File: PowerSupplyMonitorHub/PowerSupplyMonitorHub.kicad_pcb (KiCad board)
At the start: 2 copper layers, 145 x 62 mm, 97 parts, among them J1 PCA, J10 Input, J2 RJ45 PWR 0, J3 RJ45 PWR 1, J4 RJ45 PWR 2, J5 RJ45 PWR 3, J6 RJ45 PWR 4, J7 OLED I2C, J8 TCA, J9 PCF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

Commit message: added minimal readme
added many vias for ground front and back plane
updated 3d render of i2c hub pcb
updated gerber archive files
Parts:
- moved C1 1.14 mm to (108.6, 118.9), turned to 270 degrees
- moved C3 0.64 mm to (200.9, 118.2)
- turned R13 to 180 degrees
- turned R14 to 180 degrees
- turned R15 to 180 degrees
- turned R9 to 180 degrees
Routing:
- net +5V: track 467.5 -> 447.7 mm, vias 2 -> 3
- net /LINK_4: track 156.8 -> 170.0 mm, vias 0 -> 2
- net /DC-OK_0: track 33.3 -> 25.2 mm, vias 0 -> 2
- net GND: track 0.00 -> 7.65 mm, vias 0 -> 29
- net Net-(J8-Pad3): track 14.7 -> 7.96 mm, vias 0 -> 1
- net /RC_3: track 49.3 -> 56.0 mm
- net /DC-OK_4: track 19.9 -> 24.8 mm
- net /RC_1: track 22.8 -> 27.5 mm
- net Net-(J8-Pad5): track 13.2 -> 8.60 mm, vias 0 -> 1
- net /DATA_3: track 109.3 -> 113.7 mm
- net /DC-OK_1: track 20.0 -> 24.3 mm, vias 0 -> 2
- net /DATA_4: track 175.7 -> 179.6 mm
- net /RC_0: track 47.1 -> 43.2 mm, vias 0 -> 2
- net /SDA1: track 68.5 -> 72.0 mm
- net /SCL0: track 94.5 -> 97.8 mm
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
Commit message: updated readme and license file
added datasheet for ads1015
added datasheet for pca9685
added foto of gy-712 30a sensor
added small changes to pcbs
updated 3d render of pcbs
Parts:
- turned R15 to 0 degrees
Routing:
- net +5V: track 447.7 -> 428.9 mm, vias 3 -> 4
- net /LINK_4: track 170.0 -> 175.1 mm
- net /RC_4: track 78.1 -> 73.6 mm, vias 0 -> 2
- net /DC-OK_4: track 24.8 -> 22.9 mm
- net /RC_2: track 25.5 -> 27.3 mm
- net Net-(R15-Pad2): track 4.13 -> 3.28 mm
- net /SDA: track 177.2 -> 177.9 mm

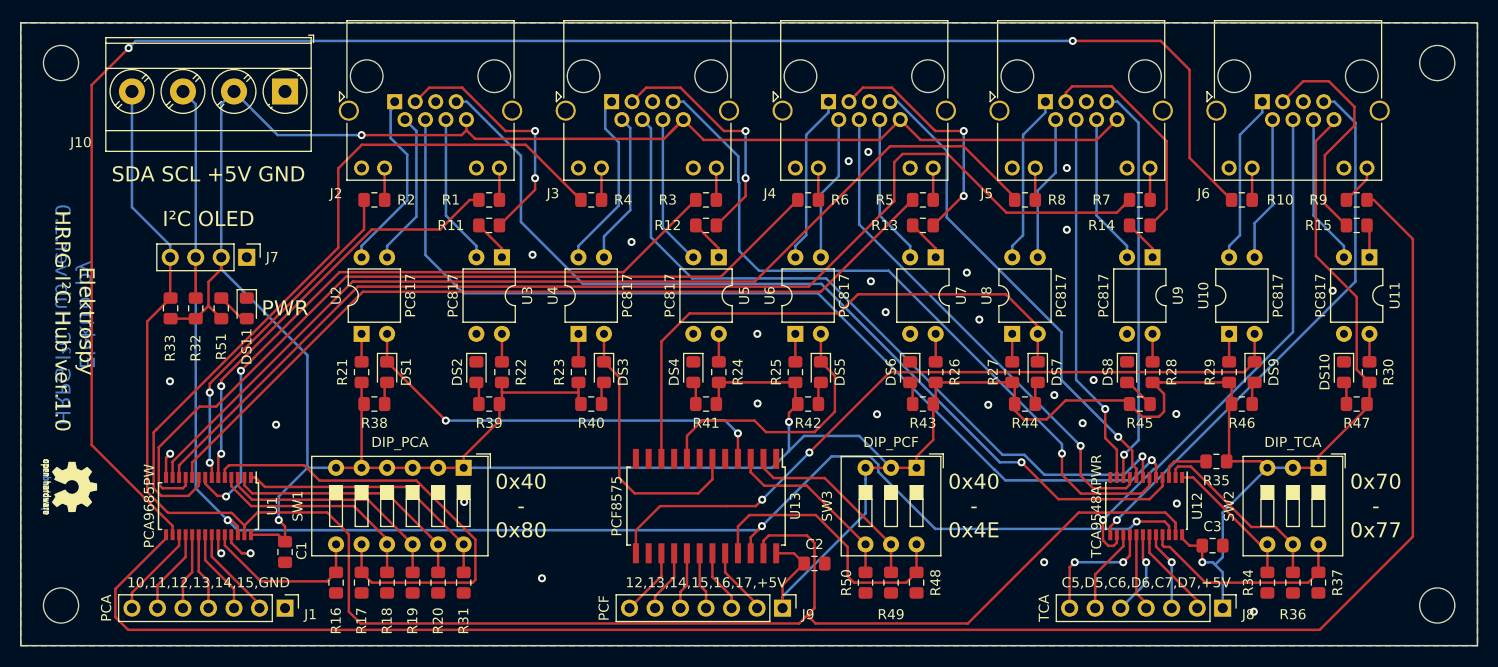
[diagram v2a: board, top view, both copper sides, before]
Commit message: fixed pcb errors
swapped gnd and vcc pin of 4 position switch to fix first two addresses
added custom 3d model for 4 position switch as step file
added custom library for 4 position switch
fixed routing of feedback signal lines (dc0-dc5)
removed double current limiting led resistors
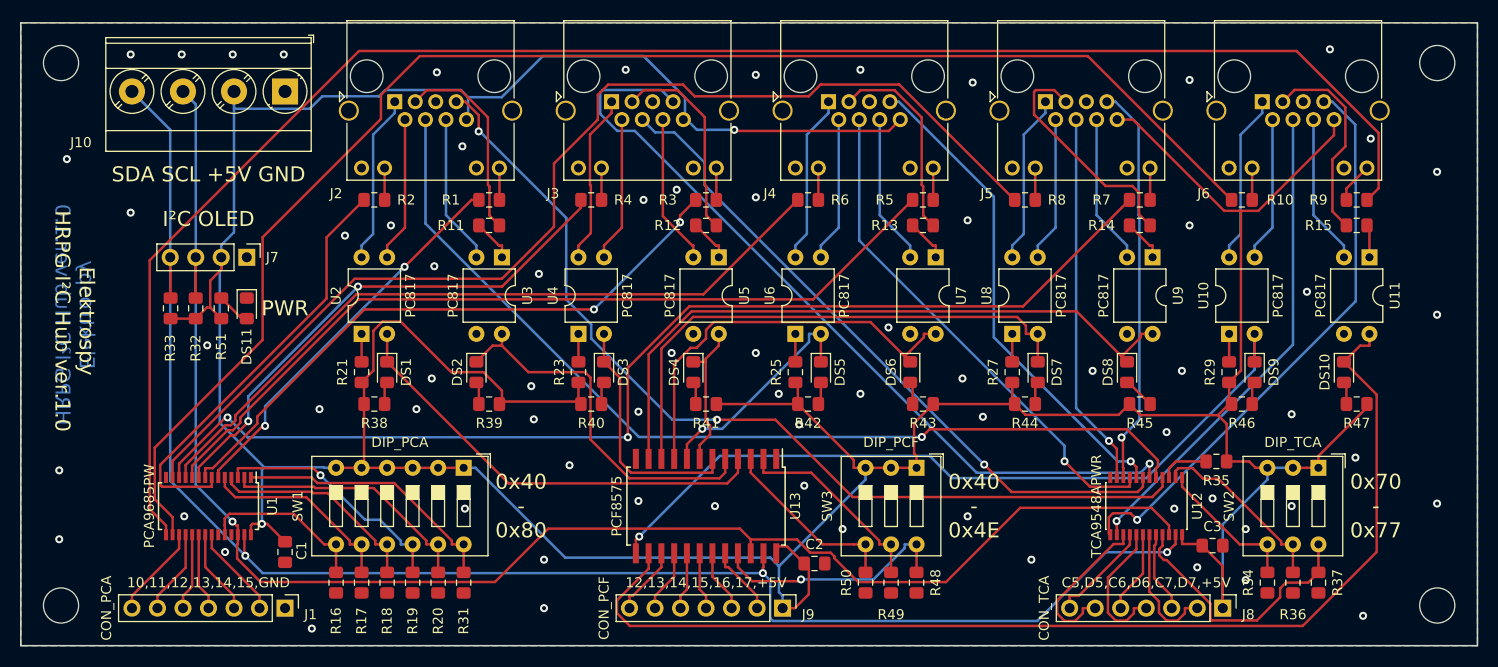
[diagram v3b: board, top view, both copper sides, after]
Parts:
- removed G***: LOGO, w_logo:Logo_silk_OSHW_6x6mm
- removed G***: LOGO, w_logo:Logo_copper_OSHW_6x6mm
- removed R22, R24, R26, R28, R30: 220, Resistor_SMD:R_0805_2012Metric_Pad1.15x1.40mm_HandSolder
- C1: value C_PCA -> 0.1uF
- C2: value C_PCF -> 0.1uF
- C3: value C_TCA -> 0.1uF
- J1: value PCA -> CON_PCA
- J8: value TCA -> CON_TCA
- J9: value PCF -> CON_PCF
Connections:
- DS10 pad 1: GND -> /DC_4
- DS2 pad 1: GND -> /DC_0
- DS4 pad 1: GND -> /DC_1
- DS6 pad 1: GND -> /DC_2
- DS8 pad 1: GND -> /DC_3
- U11 pad 4: Net-(R30-Pad1) -> /DC_4
- U13 pad 11: GND -> /DC_3
- U13 pad 14: GND -> /DC_4
- U13 pad 5: GND -> /DC_0
- U13 pad 7: GND -> /DC_1
- U13 pad 9: GND -> /DC_2
- U3 pad 4: Net-(R22-Pad1) -> /DC_0
- U5 pad 4: Net-(R24-Pad1) -> /DC_1
- U7 pad 4: Net-(R26-Pad1) -> /DC_2
- U9 pad 4: Net-(R28-Pad1) -> /DC_3
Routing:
- net /DC_4: track 0.00 -> 111.1 mm
- net /DC_3: track 0.00 -> 66.1 mm
- net /DC_2: track 0.00 -> 41.0 mm
- net /DC_0: track 0.00 -> 37.3 mm
- net /LINK_4: track 175.1 -> 146.1 mm, vias 2 -> 0
- net Net-(R17-Pad1): track 47.7 -> 19.9 mm
- net /LINK_1: track 72.9 -> 52.0 mm, vias 0 -> 2
- net /SDA: track 177.9 -> 160.7 mm, vias 0 -> 3
- net /DC_1: track 0.00 -> 14.8 mm
- net /LINK_3: track 100.8 -> 111.8 mm
- net /DATA_4: track 179.6 -> 169.5 mm
- net /SDA1: track 72.0 -> 81.2 mm
- net /LINK_0: track 34.1 -> 42.9 mm, vias 2 -> 0
- net /LINK_2: track 81.3 -> 73.4 mm
- net GND: track 7.65 -> 0.00 mm, vias 29 -> 69
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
